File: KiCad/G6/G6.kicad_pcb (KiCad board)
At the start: 2 copper layers, 0 parts

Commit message: im sorry parsa :/
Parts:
- added C10: .1uf, CC0603KRXQRQBB104:.1CAP_CC1206_YAG, F.Cu at (116.6, 70.7)
- added C11: 2.2uf, CC0603KRXQRQBB104:2.2CAP_CC1206_YAG, F.Cu at (113.6, 70.7)
- added C18: .01uF, CC0603KRXQRQBB104:.01YAG_CC1206_YAG, F.Cu at (128.5, 105.0)
- added C19: .1uF, CC0603KRXQRQBB104:.1CAP_CC1206_YAG, F.Cu at (151.3, 88.3)
- added C2: .1uF, CC0603KRXQRQBB104:.1CAP_CC1206_YAG, F.Cu at (106.2, 85.7)
- added C3: .1uF, CC0603KRXQRQBB104:.1CAP_CC1206_YAG, F.Cu at (106.2, 82.7)
- added C4: 10uF, CC0603KRXQRQBB104:10CAPC370195_195N_KEM-L, F.Cu at (116.9, 105.4)
- added C5: 1uF, CC0603KRXQRQBB104:1CAP_CS1206_YAG, F.Cu at (119.9, 105.4)
- added C6: .01uf, CC0603KRXQRQBB104:.01YAG_CC1206_YAG, F.Cu at (125.6, 70.7)
- added C7: .1uf, CC0603KRXQRQBB104:.1CAP_CC1206_YAG, F.Cu at (129.6, 70.7)
- added C8: 2.2uf, CC0603KRXQRQBB104:2.2CAP_CC1206_YAG, F.Cu at (132.6, 70.7)
- added C9: .01uf, CC0603KRXQRQBB104:.01YAG_CC1206_YAG, F.Cu at (120.6, 70.7)
- added D1: IR26-21C_L110_TR8, LED_SMD:LED_1206_3216Metric, F.Cu at (76.5, 97.1)
- added E1: YG0043AA, YG0043AA:XDCR_YG0043AA, F.Cu at (106.2, 137.8)
- added IC1: BGU7004,115, BGU7004:BGU7004115, B.Cu at (128.2, 131.3)
- added IC2: LD56020M180R, Package_TO_SOT_SMD:SOT-23-5, B.Cu at (128.4, 125.6)
- added J1: Conn_02x10_Odd_Even, Connector_PinHeader_2.54mm:PinHeader_2x10_P2.54mm_Vertical, F.Cu at (119.3, 38.8)
- added L1: 5.6nH, Inductor_SMD:L_1206_3216Metric, B.Cu at (123.0, 125.6)
- added Q1: 2N3904, Package_TO_SOT_THT:TO-92_Inline, F.Cu at (75.7, 92.8)
- added R10: 10k, Resistor_SMD:R_1206_3216Metric, F.Cu at (70.9, 91.2)
- added R11: 1k, Resistor_SMD:R_1206_3216Metric, F.Cu at (70.9, 94.5)
- added R12: 1k, Resistor_SMD:R_1206_3216Metric, F.Cu at (70.9, 97.8)
- added R5: RC1206FR-0724RL, Resistor_SMD:R_1206_3216Metric, F.Cu at (170.2, 147.5)
- added R6: 10k, CC0603KRXQRQBB104:10kRC1206N_YAG, F.Cu at (151.3, 91.3)
- added R7: RC1206FR-0724RL, Resistor_SMD:R_1206_3216Metric, F.Cu at (157.7, 147.5)
- added U1: STM32C051K8T6, CC0603KRXQRQBB104:LQFP32_7x7_STM, F.Cu at (122.5, 86.8)
- added U11: SN74HC74DRG4 (SOIC14), Package_SO:SOIC-14_3.9x8.7mm_P1.27mm, F.Cu at (72.3, 77.8)
- added U12: ~, CC0603KRXQRQBB104:RSF-1575.420-24000-3030-TR, B.Cu at (123.0, 132.4)
- added U13: IIM-42653, CC0603KRXQRQBB104:IIM42563, F.Cu at (125.6, 75.7)
- added U14: IIM-42653, CC0603KRXQRQBB104:IIM42563, F.Cu at (120.6, 75.7)
- added U15: TMP127EDBVRQ1, CC0603KRXQRQBB104:SOT23_DBV_TEX, F.Cu at (141.3, 89.6)
- added U2: NEO-M9N-00B, NEO_M9N_00B:XCVR_NEO-M9N-00B, B.Cu at (129.6, 143.4)
- added U3: BMI270 - Secondary Accelerometer, BMI270 (1):XDCR_BMI270, F.Cu at (111.0, 83.6)
- added U4: MMC5983MA-Magnetomer, MMC5983MA:PQFN50P300X300X100-16N, F.Cu at (118.5, 100.0)
- added U5: MS560702BA03-50 - Barometer, MS560702BA03_50 (1):SON125P300X500X100-8N, F.Cu at (128.5, 100.0)
- added U7: SN65HVD74DR, 2N65HVD74DR:D8_TEX, F.Cu at (160.9, 140.9)
- added U8: ISL83488IBZ, CC0603KRXQRQBB104:SOIC8_4X5_INR, F.Cu at (91.4, 109.0)

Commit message: not albino tiger shark
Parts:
- removed E1: YG0043AA, YG0043AA:XDCR_YG0043AA
- moved U13 2.71 mm to (127.7, 77.4)
- moved U1 1.36 mm to (123.8, 87.4), turned to 45 degrees

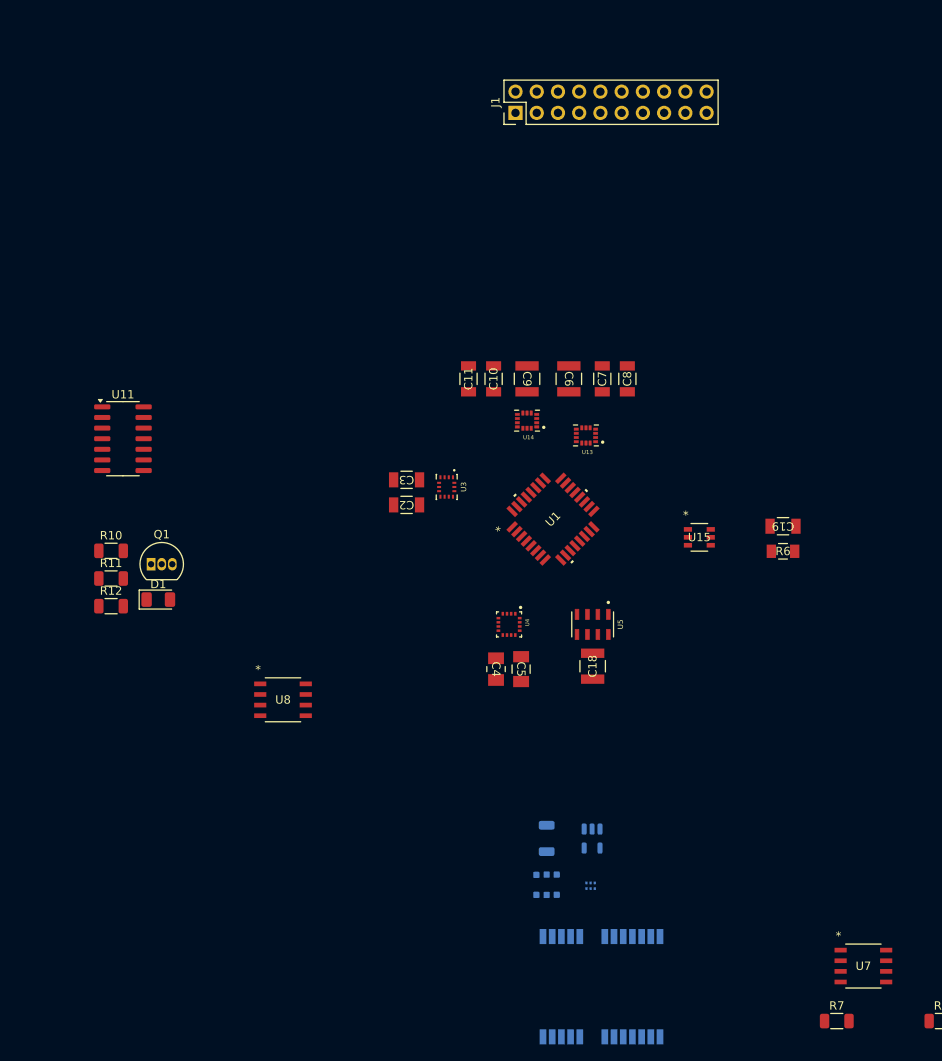
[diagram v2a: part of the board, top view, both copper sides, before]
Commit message: errrrrr i cant find a umcx connector they all say there like $50??
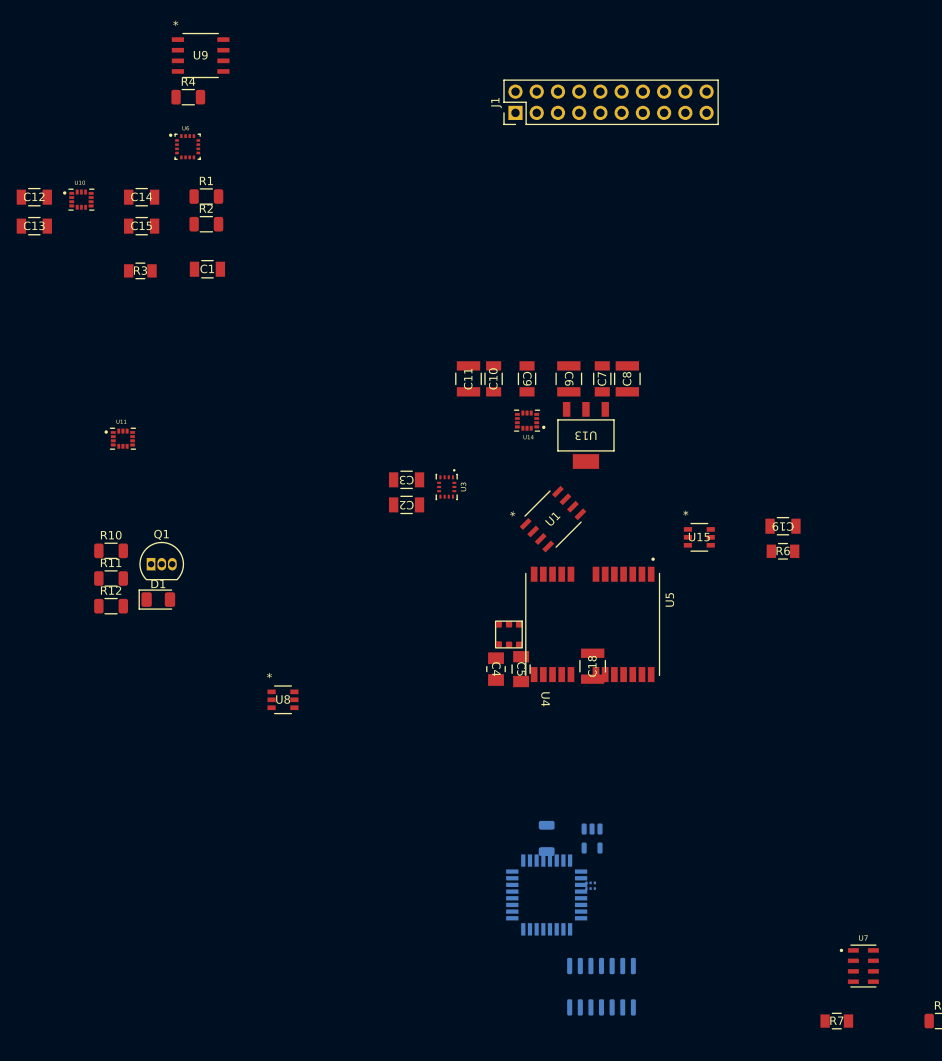
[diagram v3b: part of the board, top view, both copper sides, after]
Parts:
- added C1: .1uF, CC0603KRXQRQBB104:.1CAP_CC1206_YAG, F.Cu at (82.4, 57.5)
- added C12: .1uf, CC0603KRXQRQBB104:.1CAP_CC1206_YAG, F.Cu at (61.7, 48.9)
- added C13: 2.2uf, CC0603KRXQRQBB104:2.2CAP_CC1206_YAG, F.Cu at (61.7, 52.4)
- added C14: .1uf, CC0603KRXQRQBB104:.1CAP_CC1206_YAG, F.Cu at (74.5, 48.9)
- added C15: .1uf, CC0603KRXQRQBB104:.1CAP_CC1206_YAG, F.Cu at (74.5, 52.4)
- added R1: 1k, Resistor_SMD:R_1206_3216Metric, F.Cu at (82.3, 48.8)
- added R2: 1k, Resistor_SMD:R_1206_3216Metric, F.Cu at (82.3, 52.1)
- added R3: 10k, CC0603KRXQRQBB104:10kRC1206N_YAG, F.Cu at (74.4, 57.7)
- added R4: RC1206FR-0724RL, Resistor_SMD:R_1206_3216Metric, F.Cu at (80.1, 37.0)
- added U10: IIM-42653, CC0603KRXQRQBB104:IIM42563, F.Cu at (67.3, 49.2)
- added U6: MMC5983MA-Magnetomer, MMC5983MA:PQFN50P300X300X100-16N, F.Cu at (80.0, 42.9)
- added U9: SN65HVD74DR, 2N65HVD74DR:D8_TEX, F.Cu at (81.6, 32.0)
- C10: value .1uf -> 2.2uf; footprint CC0603KRXQRQBB104:.1CAP_CC1206_YAG -> CC0603KRXQRQBB104:2.2CAP_CC1206_YAG
- C11, C8: value 2.2uf -> .01uf; footprint CC0603KRXQRQBB104:2.2CAP_CC1206_YAG -> CC0603KRXQRQBB104:.01YAG_CC1206_YAG
- C3: value .1uF -> 0.1
- C6: value .01uf -> .01uF
- C7: value .1uf -> .1uF
- C9: value .01uf -> .1uf; footprint CC0603KRXQRQBB104:.01YAG_CC1206_YAG -> CC0603KRXQRQBB104:.1CAP_CC1206_YAG
- R7: value RC1206FR-0724RL -> 10k; footprint Resistor_SMD:R_1206_3216Metric -> CC0603KRXQRQBB104:10kRC1206N_YAG
- U1: value STM32C051K8T6 -> ISL83488IBZ; footprint CC0603KRXQRQBB104:LQFP32_7x7_STM -> CC0603KRXQRQBB104:SOIC8_4X5_INR
- U11: value SN74HC74DRG4 (SOIC14) -> IIM-42653; footprint Package_SO:SOIC-14_3.9x8.7mm_P1.27mm -> CC0603KRXQRQBB104:IIM42563
- U12: value ~ -> STM32C051K8T6; footprint CC0603KRXQRQBB104:RSF-1575.420-24000-3030-TR -> CC0603KRXQRQBB104:LQFP32_7x7_STM
- U13: value IIM-42653 -> REG1117A-1.8; footprint CC0603KRXQRQBB104:IIM42563 -> CC0603KRXQRQBB104:LDO1.8
- U2: value NEO-M9N-00B -> SN74HC74DRG4 (SOIC14); footprint NEO_M9N_00B:XCVR_NEO-M9N-00B -> Package_SO:SOIC-14_3.9x8.7mm_P1.27mm
- U4: value MMC5983MA-Magnetomer -> ~; footprint MMC5983MA:PQFN50P300X300X100-16N -> CC0603KRXQRQBB104:RSF-1575.420-24000-3030-TR
- U5: value MS560702BA03-50 - Barometer -> NEO-M9N-00B; footprint MS560702BA03_50 (1):SON125P300X500X100-8N -> NEO_M9N_00B:XCVR_NEO-M9N-00B
- U7: value SN65HVD74DR -> MS560702BA03-50 - Barometer; footprint 2N65HVD74DR:D8_TEX -> MS560702BA03_50 (1):SON125P300X500X100-8N
- U8: value ISL83488IBZ -> TMP127EDBVRQ1; footprint CC0603KRXQRQBB104:SOIC8_4X5_INR -> CC0603KRXQRQBB104:SOT23_DBV_TEX
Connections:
- C10 pad 2: GNDD -> GND
- C11 pad 1: 3.3v -> GND
- C11 pad 2: GNDD -> 3.3v
- C2 pad 2: GNDD -> GND
- C3 pad 1: 3.3v -> GND
- C3 pad 2: GNDD -> 3.3v
- C4 pad 1: Net-(U4-CAP) -> Net-(U6-CAP)
- C4 pad 2: GNDD -> GND
- C5 pad 2: GNDD -> GND
- C7 pad 1: 3.3v -> GND
- C7 pad 2: GNDD -> 3.3v
- C8 pad 1: 3.3v -> GND
- C8 pad 2: GNDD -> 3.3v
- C9 pad 1: GNDD -> 3.3v
- C9 pad 2: 3.3v -> GND
- IC1 pad 1: GNDD -> GND
- IC1 pad 2: GNDD -> GND
- L1 pad 1: Net-(U12-5_Rf_output) -> Net-(U4-5_Rf_output)
- Q1 pad 1: GNDD -> GND
- R5 pad 1: a+ -> y+
- R5 pad 2: a- -> y-
- R6 pad 1: /BMI270/MOSI-BMI -> 3.3v
- R6 pad 2: /BMI270/MISO-BMI -> Net-(U12-PF2-NRST)
- R7 pad 1: y+ -> 3.3v
- R7 pad 2: y- -> Net-(U12-PA13)
- U1 pad 1: /BMI270/CS-BMI -> 3.3v
- U1 pad 8: /BMI270/SCK-MAIN -> unconnected-(U1-A-Pad8)
- U11 pad 1: Net-(U11-VDD) -> /BMI270/MISO-BMI
- U11 pad 12: unconnected-(U11-RA1-Pad12) -> /IIM-42653/CS-IIM2
- U11 pad 13: unconnected-(U11-RA0-Pad13) -> /SCK-MAIN
- U11 pad 14: 3.3v -> /BMI270/MOSI-BMI
- U11 pad 2: Net-(U11-RA5) -> unconnected-(U11-AUX1_SDIO-Pad2)
- U11 pad 3: PPS -> unconnected-(U11-AUX1_SCLK-Pad3)
- U11 pad 5: Net-(U11-RC5) -> 3.3v
- U11 pad 6: Net-(U11-RA5) -> Net-(U11-GND)
- U11 pad 7: GNDD -> Net-(U11-GND)
- U11 pad 8: unconnected-(U11-RC2-Pad8) -> 3.3v
- U12 pad 1: GNDD -> /BMI270/CS-BMI
- U12 pad 2: Net-(U12-2_Rf_in) -> unconnected-(U12-PC14-OSCX_IN-Pad2)
- U12 pad 3: GNDD -> unconnected-(U12-PC15-OSCX_OUT-Pad3)
- U12 pad 4: GNDD -> 3.3v
- U12 pad 5: Net-(U12-5_Rf_output) -> GND
- U12 pad 6: GNDD -> Net-(U12-PF2-NRST)
- U13 pad 1: /BMI270/MOSI-BMI -> GND
- U13 pad 3: unconnected-(U13-AUX1_SCLK-Pad3) -> 3.3v
- U13 pad 4: unconnected-(U13-INT1/INT-Pad4) -> Net-(IC1-VCC)
- U2 pad 1: unconnected-(U2-SAFEBOOT_N-Pad1) -> 3.3v
- U2 pad 10: GNDD -> unconnected-(U2-RC0-Pad10)
- U2 pad 11: Net-(IC1-RF_OUT) -> unconnected-(U2-RA2-Pad11)
- U2 pad 12: GNDD -> unconnected-(U2-RA1-Pad12)
- U2 pad 13: GNDD -> unconnected-(U2-RA0-Pad13)
- U2 pad 14: unconnected-(U2-LNA_EN-Pad14) -> GND
- U2 pad 2: 3.3v -> Net-(U2-RA5)
- U2 pad 5: unconnected-(U2-USB_DM-Pad5) -> Net-(U2-RC5)
- U2 pad 6: unconnected-(U2-USB_DP-Pad6) -> Net-(U2-RA5)
- U2 pad 8: GPIO -> unconnected-(U2-RC2-Pad8)
- U3 pad 10: GNDD -> GND
- U3 pad 11: GNDD -> GND
- U3 pad 13: /BMI270/SCK-MAIN -> /SCK-MAIN
- U3 pad 6: GNDD -> GND
- U3 pad 7: GNDD -> GND
- U4 pad 1: /BMI270/SCK-MAIN -> GNDD
- U4 pad 2: 3.3v -> Net-(U4-2_Rf_in)
- U4 pad 3: unconnected-(U4-NC-Pad3) -> GNDD
- U4 pad 4: /MMC5983/CS-MMC -> GNDD
- U4 pad 5: /BMI270/MISO-BMI -> Net-(U4-5_Rf_output)
- U4 pad 6: unconnected-(U4-NC__1-Pad6) -> GNDD
- U5 pad 1: 3.3v -> unconnected-(U5-SAFEBOOT_N-Pad1)
- U5 pad 2: GNDD -> GND
- U5 pad 3: GNDD -> /GPS/PPS
- U5 pad 4: /MS560702/CS-MS5 -> unconnected-(U5-EXTINT-Pad4)
- U5 pad 5: GNDD -> unconnected-(U5-USB_DM-Pad5)
- U5 pad 6: /BMI270/MISO-BMI -> unconnected-(U5-USB_DP-Pad6)
- U5 pad 7: /BMI270/MOSI-BMI -> unconnected-(U5-V_USB-Pad7)
- U5 pad 8: /BMI270/SCK-MAIN -> /GPS/GPIO
- U7 pad 2: R -> GNDD
- U7 pad 3: T -> GNDD
- U7 pad 4: GNDD -> /MS560702/CS-MS5
- U7 pad 5: y+ -> GNDD
- U7 pad 6: y- -> /BMI270/MISO-BMI
- U7 pad 7: a- -> /BMI270/MOSI-BMI
- U7 pad 8: a+ -> /SCK-MAIN
- U8 pad 1: unconnected-(U8-VCC-Pad1) -> /STM/CS-TMP
- U8 pad 2: unconnected-(U8-RO-Pad2) -> GND
- U8 pad 3: unconnected-(U8-DI-Pad3) -> /BMI270/MISO-BMI
- U8 pad 4: unconnected-(U8-GND-Pad4) -> /SCK-MAIN
- U8 pad 6: unconnected-(U8-Z-Pad6) -> 3.3v

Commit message: i have no idea whats going on, everything crashed and nothing will open
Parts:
- removed IC2: LD56020M180R, Package_TO_SOT_SMD:SOT-23-5
- removed R4: RC1206FR-0724RL, Resistor_SMD:R_1206_3216Metric
- removed U14: IIM-42653, CC0603KRXQRQBB104:IIM42563
- removed U15: TMP127EDBVRQ1, CC0603KRXQRQBB104:SOT23_DBV_TEX
- removed U9: SN65HVD74DR, 2N65HVD74DR:D8_TEX
- added R8: RC1206FR-0724RL, Resistor_SMD:R_1206_3216Metric, F.Cu at (179.2, 57.0)
- added R9: RC1206FR-0724RL, Resistor_SMD:R_1206_3216Metric, F.Cu at (179.2, 60.3)
- IC1, L1, U12, U2: moved to F.Cu
- moved U2 82.8 mm to (75.4, 80.7)
- moved R3 75.3 mm to (136.9, 99.6), turned to 180 degrees
- moved U6 74.5 mm to (122.9, 103.8), turned to -90 degrees
- moved C12 72.4 mm to (128.6, 76.5), turned to 90 degrees
- moved C13 68.3 mm to (125.6, 76.5), turned to 90 degrees
- moved U10 63.2 mm to (121.6, 81.5), turned to 180 degrees
- moved U13 60.6 mm to (139.1, 136.9)
- moved U11 57.5 mm to (129.6, 81.5), turned to 180 degrees
- moved U1 53.3 mm to (174.4, 70.8)
- moved U7 48.4 mm to (129.5, 104.1), turned to -90 degrees
- moved U8 47.3 mm to (136.9, 96.1)
- moved C1 45.3 mm to (111.8, 92.0), turned to 180 degrees
- moved U5 39.4 mm to (119.5, 138.4), turned to 0 degrees
- moved U12 39.3 mm to (125.7, 93.2), turned to 0 degrees
- moved C6 38.5 mm to (133.3, 108.4), turned to 180 degrees
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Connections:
- U1 pad 2: unconnected-(U1-RO-Pad2) -> /Transceiver/RX
- U1 pad 3: unconnected-(U1-DI-Pad3) -> /Transceiver/TX
- U1 pad 4: unconnected-(U1-GND-Pad4) -> GND
- U1 pad 5: unconnected-(U1-Y-Pad5) -> y+
- U1 pad 6: unconnected-(U1-Z-Pad6) -> y-
- U1 pad 7: unconnected-(U1-B-Pad7) -> a-
- U1 pad 8: unconnected-(U1-A-Pad8) -> a+
- U11 pad 6: Net-(U11-GND) -> GND
- U11 pad 7: Net-(U11-GND) -> GND
- U12 pad 13: unconnected-(U12-PA6-Pad13) -> /STM/TX
- U12 pad 14: unconnected-(U12-PA7-Pad14) -> /STM/RX
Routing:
- net /BMI270/MISO-BMI: track 0.00 -> 71.1 mm, vias 0 -> 8
- net /BMI270/MOSI-BMI: track 0.00 -> 65.5 mm, vias 0 -> 11
- net 3.3v: track 0.00 -> 56.5 mm
- net /SCK-MAIN: track 0.00 -> 50.3 mm, vias 0 -> 6
- net /IIM-42653/CS-IIM1: track 0.00 -> 11.0 mm
- net /IIM-42653/CS-IIM2: track 0.00 -> 7.30 mm
- net /MMC5983/CS-MMC: track 0.00 -> 6.20 mm
- net /STM/CS-TMP: track 0.00 -> 5.68 mm
- net /MS560702/CS-MS5: track 0.00 -> 5.58 mm
- net /BMI270/CS-BMI: track 0.00 -> 4.28 mm
- net Net-(U6-CAP): track 0.00 -> 2.80 mm
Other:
- copper layers 2 -> 4

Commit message: idk whats going on anymore
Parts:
- removed C18: .01uF, CC0603KRXQRQBB104:.01YAG_CC1206_YAG
- removed C19: .1uF, CC0603KRXQRQBB104:.1CAP_CC1206_YAG
- removed R10: 10k, Resistor_SMD:R_1206_3216Metric
- removed R11, R12: 1k, Resistor_SMD:R_1206_3216Metric
- removed R5: RC1206FR-0724RL, Resistor_SMD:R_1206_3216Metric
- added C16: 22pf, Capacitor_SMD:C_1206_3216Metric, F.Cu at (114.6, 92.8)
- added C17: 22pf, Capacitor_SMD:C_1206_3216Metric, F.Cu at (114.6, 90.3)
- added Y1: ABS07-32.768KHZ-1-T, CC0603KRXQRQBB104:XTAL_ABS07-32.768KHZ-1-T, F.Cu at (118.6, 91.6)
- moved R2 89.1 mm to (75.7, 141.0)
- moved R1 88.8 mm to (76.6, 137.4)
- moved U13 87.3 mm to (127.8, 50.3), turned to -90 degrees
- moved U5 81.4 mm to (140.7, 59.8), turned to -90 degrees
- moved U4 80.8 mm to (141.3, 47.0), turned to 180 degrees
- moved L1 78.6 mm to (135.3, 47.0), turned to 180 degrees
- moved IC1 76.9 mm to (134.8, 50.3), turned to 180 degrees
- moved C3 72.9 mm to (147.6, 68.8)
- moved R7 62.0 mm to (133.6, 90.4), turned to 180 degrees
- moved C15 54.2 mm to (103.8, 98.0)
- moved R6 48.5 mm to (103.8, 101.0)
- moved Q1 46.8 mm to (81.5, 139.2)
- moved D1 46.8 mm to (82.4, 143.5)
- moved U2 46.8 mm to (81.2, 127.1)
- moved C14 46.7 mm to (103.8, 95.0)
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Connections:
- U12 pad 2: unconnected-(U12-PC14-OSCX_IN-Pad2) -> Net-(U12-PC14-OSCX_IN)
- U12 pad 3: unconnected-(U12-PC15-OSCX_OUT-Pad3) -> Net-(U12-PC15-OSCX_OUT)
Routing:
- net /SCK-MAIN: track 50.3 -> 82.3 mm
- net Net-(U12-PF2-NRST): track 0.00 -> 27.9 mm
- net 3.3v: track 56.5 -> 78.8 mm
- net /BMI270/MOSI-BMI: track 65.5 -> 81.2 mm
- net /BMI270/CS-BMI: track 4.28 -> 12.3 mm, vias 0 -> 2
- net /BMI270/MISO-BMI: track 71.1 -> 79.1 mm
- net Net-(U12-PC15-OSCX_OUT): track 0.00 -> 5.86 mm
- net Net-(U12-PC14-OSCX_IN): track 0.00 -> 5.86 mm
- net y-: track 0.00 -> 5.67 mm
- net a-: track 0.00 -> 5.67 mm
- net y+: track 0.00 -> 5.13 mm
- net a+: track 0.00 -> 5.13 mm
- net Net-(IC1-VCC): track 0.00 -> 3.52 mm
- net Net-(IC1-RF_OUT): track 0.00 -> 3.37 mm
- net Net-(IC1-RF_IN): track 0.00 -> 3.24 mm
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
